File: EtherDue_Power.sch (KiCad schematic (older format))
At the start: 46 parts, among them Q501 BC847BSMD, U203 LMV358IDGKR, U501 POWERJACK, U502 LM2734Y, U503 FDN340P, U504 FDN340P, U505 NCP1117ST33T3G

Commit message: Add note about DC Input voltages to schematic
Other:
- note added: "7-12V Recommended,\n6-20V Possible."
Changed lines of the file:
@@
 Sheet 7 7
 Title "EtherDue"
-Date "16 jan 2014"
+Date "13 mar 2014"
 Rev ""
 Comp "(C) 2014 Freetronics Pty Ltd"
@@
 Wire Wire Line
 	7150 6950 9350 6950
+Text Notes 700  2100 0    60   ~ 0
+7-12V Recommended,\n6-20V Possible.
 $EndSCHEMATC

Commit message: Fix wrong footprint LMV358IDGKR to TSSOP footprint LMV385IPWR
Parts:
- U203: value LMV358IDGKR -> LMV358IPWR
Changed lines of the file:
@@
 P 5300 4700
 F 0 "U203" H 5250 4900 60  0000 L CNN
-F 1 "LMV358IDGKR" H 5250 4450 60  0000 L CNN
+F 1 "LMV358IPWR" H 5250 4450 60  0000 L CNN
 F 2 "" H 5300 4700 60  0001 C CNN
 F 3 "" H 5300 4700 60  0001 C CNN

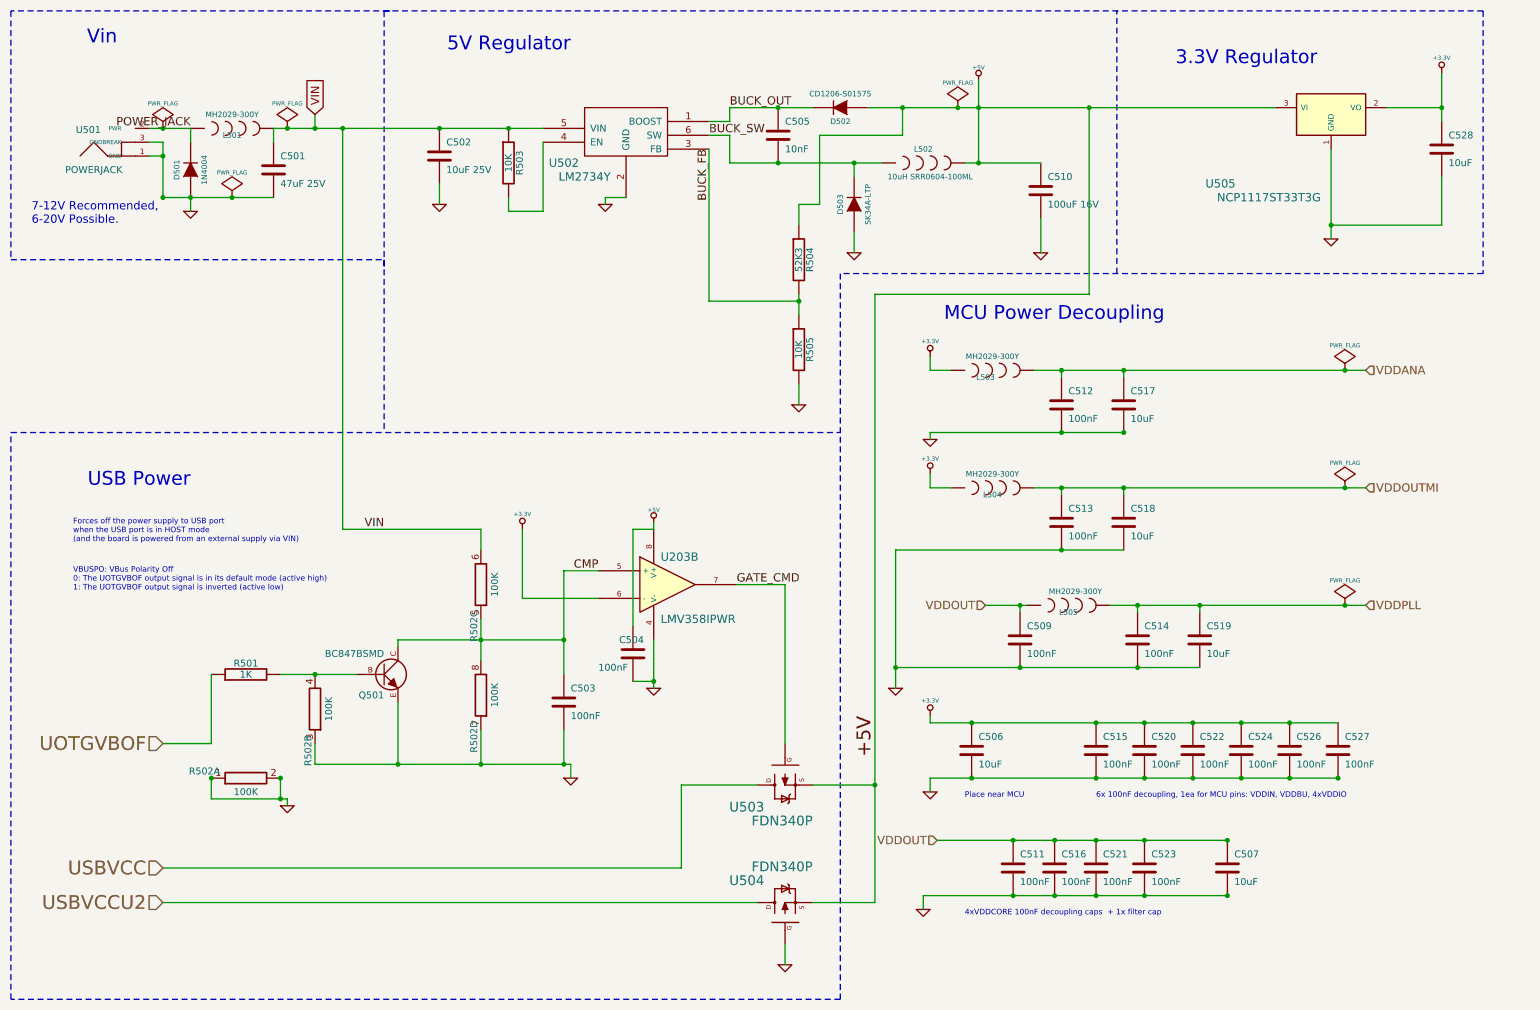
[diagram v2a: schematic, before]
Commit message: Update EtherDue from Kicad 2013-07 to 2014-07 (incl. "pretty" footprints, etc.)
New netlist has been imported into PCB but new "pretty" footprint
associations HAVE NOT, need to take care if replacing any of these
from the new libraries as associations may be different.
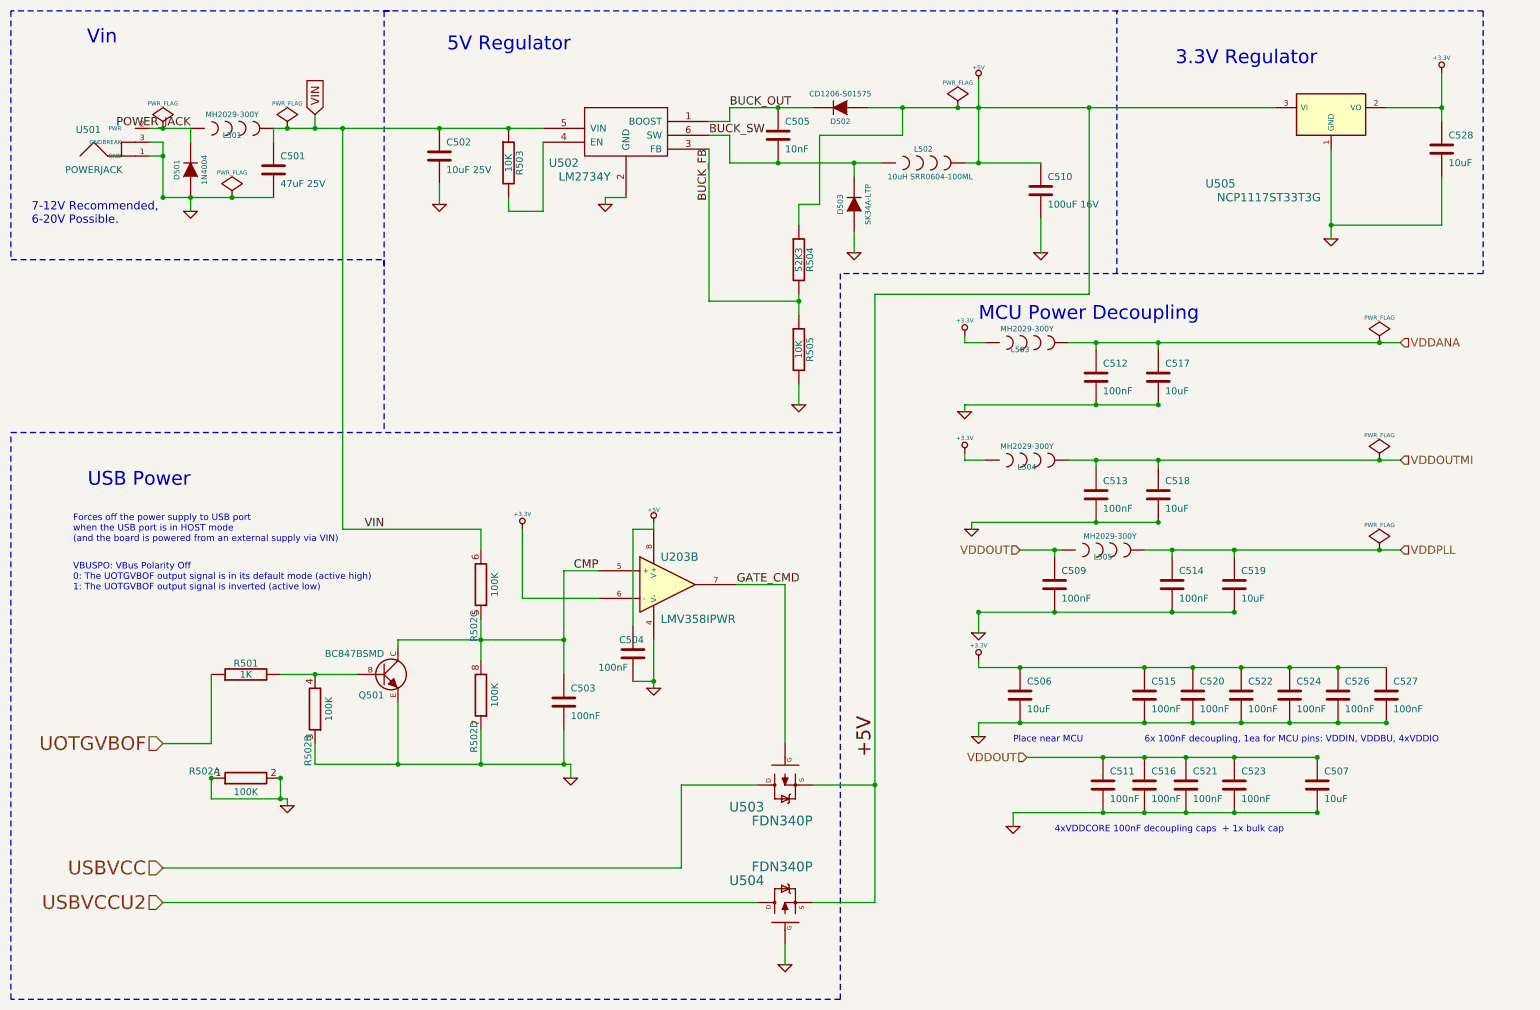
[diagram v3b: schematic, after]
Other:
- note added: "4xVDDCORE 100nF decoupling caps + 1x bulk cap\n"
- note removed: "4xVDDCORE 100nF decoupling caps + 1x filter cap\n"
- moved on the sheet: C506, C507, C509, C511, C512, C513, C514, C515, C516, C517, C518, C519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
